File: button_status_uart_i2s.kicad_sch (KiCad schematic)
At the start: 14 parts, among them CN10 JST_ZH_6PIN_1A_250V, CN8 4P JST ZH, CN9 4P JST ZH

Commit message: commit before updating to LiveAstra lib
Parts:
- added R9: 10k, Resistor_SMD:R_0402_1005Metric, symbol EASYEDA2KICAD:R_10kOhm_0402_62mW
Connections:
- net GPIO_12_BUTTON: now also R9.2; no longer CN9.2
- net STATUS_LED_CONN: now reaches CN9.4, R33.2
- new net: CN9.2, R9.1
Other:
- moved on the sheet: R33
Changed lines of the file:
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@@
 	(paper "A4")
+	(junction
+		(at 127 66.04)
+		(diameter 0)
+		(color 0 0 0 0)
+	)
 	(junction
 		(at 88.9 121.92)
@@
 	)
 	(junction
-		(at 88.9 66.04)
+		(at 101.6 66.04)
 		(diameter 0)
 		(color 0 0 0 0)
 	)
 	(junction
-		(at 127 66.04)
+		(at 88.9 66.04)
 		(diameter 0)
 		(color 0 0 0 0)
@@
 	)
 	(junction
-		(at 101.6 66.04)
-		(diameter 0)
-		(color 0 0 0 0)
-	)
-	(junction
 		(at 88.9 154.94)
 		(diameter 0)
@@
 	(wire
 		(pts
-			(xy 127 66.04) (xy 167.64 66.04)
+			(xy 127 66.04) (xy 132.08 66.04)
 		)
 		(stroke
@@
 	(wire
 		(pts
-			(xy 88.9 96.52) (xy 114.3 96.52)
+			(xy 88.9 96.52) (xy 109.22 96.52)
 		)
 		(stroke
@@
 	(wire
 		(pts
+			(xy 142.24 66.04) (xy 167.64 66.04)
+		)
+		(stroke
+			(width 0)
+			(type default)
+		)
+	)
+	(wire
+		(pts
 			(xy 88.9 121.92) (xy 167.64 121.92)
 		)
@@
 	(wire
 		(pts
+			(xy 101.6 66.04) (xy 127 66.04)
+		)
+		(stroke
+			(width 0)
+			(type default)
+		)
+	)
+	(wire
+		(pts
 			(xy 127 81.28) (xy 127 78.74)
 		)
@@
 	(wire
 		(pts
-			(xy 101.6 66.04) (xy 127 66.04)
-		)
-		(stroke
-			(width 0)
-			(type default)
-		)
-	)
-	(wire
-		(pts
 			(xy 88.9 93.98) (xy 88.9 96.52)
 		)
@@
 	(wire
 		(pts
-			(xy 124.46 96.52) (xy 162.56 96.52)
+			(xy 119.38 96.52) (xy 162.56 96.52)
 		)
 		(stroke
@@
 			(width 0)
 			(type default)
+		)
+	)
+	(label "STATUS_LED_CONN"
+		(at 127 96.52 0)
+		(fields_autoplaced yes)
+		(effects
+			(font
+				(size 1.27 1.27)
+			)
+			(justify left bottom)
 		)
 	)
@@
 		(on_board yes)
 		(dnp no)
-		(property "Reference" "#PWR079"
+		(property "Reference" "#PWR79"
 			(at 142.24 113.03 0)
 			(effects
@@
 			(project "AstraControl"
 				(path "/9a751838-dce8-4d69-8a02-736625ac74e7/0db21d8e-3390-4d67-877f-0e5d98e37848/457d2566-de00-4e8c-b469-a22ed41e6193"
-					(reference "#PWR079")
+					(reference "#PWR79")
+					(unit 1)
+				)
+			)
+		)
+	)
+	(symbol
+		(lib_id "EASYEDA2KICAD:R_10kOhm_0402_62mW")
+		(at 137.16 66.04 180)
+		(unit 1)
+		(exclude_from_sim no)
+		(in_bom yes)
+		(on_board yes)
+		(dnp no)
+		(fields_autoplaced yes)
+		(property "Reference" "R9"
+			(at 137.16 57.15 0)
+			(effects
+				(font
+					(size 1.27 1.27)
+				)
+			)
+		)
+		(property "Value" "10k"
+			(at 137.16 59.69 0)
+			(effects
+				(font
+					(size 1.27 1.27)
+					(bold yes)
+				)
+			)
+		)
+		(property "Footprint" "Resistor_SMD:R_0402_1005Metric"
+			(at 137.16 53.34 0)
+			(effects
+				(font
+					(size 1.27 1.27)
+				)
+				(hide yes)
+			)
+		)
+		(property "Datasheet" "https://wmsc.lcsc.com/wmsc/upload/file/pdf/v2/lcsc/2206010100_UNI-ROYAL-Uniroyal-Elec-0402WGF1002TCE_C25744.pdf"
+			(at 137.16 57.15 0)
+			(effects
+				(font
+					(size 1.27 1.27)
+				)
+				(hide yes)
+			)
+		)
+		(property "Description" "Thick Film Resistors"
+			(at 137.16 60.96 0)
+			(effects
+				(font
+					(size 1.27 1.27)
+				)
+				(hide yes)
+			)
+		)
+		(property "LCSC Part" "C25744"
+			(at 137.16 49.53 0)
+			(effects
+				(font
+					(size 1.27 1.27)
+				)
+				(hide yes)
+			)
+		)
+		(property "Extra Values" "50V ±1% 0402 62mW"
+			(at 137.16 62.23 0)
+			(effects
+				(font
+					(size 0.762 0.762)
+					(bold yes)
+				)
+			)
+		)
+		(pin "2"
+		)
+		(pin "1"
+		)
+		(instances
+			(project "AstraControl"
+				(path "/9a751838-dce8-4d69-8a02-736625ac74e7/0db21d8e-3390-4d67-877f-0e5d98e37848/457d2566-de00-4e8c-b469-a22ed41e6193"
+					(reference "R9")
 					(unit 1)
 				)
@@
 	(symbol
 		(lib_id "EASYEDA2KICAD:R_0Ohm_0805_125mW")
-		(at 119.38 96.52 0)
+		(at 114.3 96.52 0)
 		(unit 1)
 		(exclude_from_sim no)
@@
 		(dnp no)
 		(property "Reference" "R33"
-			(at 119.38 88.9 0)
+			(at 114.3 88.9 0)
 			(effects
 				(font
@@
 		)
 		(property "Value" "0"
-			(at 119.38 91.44 0)
+			(at 114.3 91.44 0)
 			(effects
 				(font
@@
 		)
 		(property "Footprint" "Resistor_SMD:R_0805_2012Metric_Pad1.20x1.40mm_HandSolder"
-			(at 119.38 109.22 0)
+			(at 114.3 109.22 0)
 			(effects
 				(font
@@
 		)
 		(property "Datasheet" "https://lcsc.com/product-detail/Chip-Resistor-Surface-Mount-UniOhm_0R-0R0-1_C17477.html"
-			(at 119.38 105.41 0)
+			(at 114.3 105.41 0)
 			(effects
 				(font
@@
 		)
 		(property "Description" "Thick Film Resistors"
-			(at 119.38 101.6 0)
+			(at 114.3 101.6 0)
 			(effects
 				(font
@@
 		)
 		(property "LCSC Part" "C17477"
-			(at 119.38 113.03 0)
+			(at 114.3 113.03 0)
 			(effects
 				(font
@@
 		)
 		(property "Extra Values" "150V ±1% 0805"
-			(at 119.38 93.98 0)
+			(at 114.3 93.98 0)
 			(effects
 				(font
@@
 		(dnp no)
 		(fields_autoplaced yes)
-		(property "Reference" "#PWR083"
+		(property "Reference" "#PWR83"
 			(at 152.4 118.11 0)
 			(effects
@@
 			(project "AstraControl"
 				(path "/9a751838-dce8-4d69-8a02-736625ac74e7/0db21d8e-3390-4d67-877f-0e5d98e37848/457d2566-de00-4e8c-b469-a22ed41e6193"
-					(reference "#PWR083")
+					(reference "#PWR83")
 					(unit 1)
 				)
@@
 		(dnp no)
 		(fields_autoplaced yes)
-		(property "Reference" "#PWR076"
+		(property "Reference" "#PWR76"
 			(at 101.6 87.63 0)
 			(effects
@@
 			(project "AstraControl"
 				(path "/9a751838-dce8-4d69-8a02-736625ac74e7/0db21d8e-3390-4d67-877f-0e5d98e37848/457d2566-de00-4e8c-b469-a22ed41e6193"
-					(reference "#PWR076")
+					(reference "#PWR76")
 					(unit 1)
 				)
@@
 		(dnp no)
 		(fields_autoplaced yes)
-		(property "Reference" "#PWR077"
+		(property "Reference" "#PWR77"
 			(at 127 87.63 0)
 			(effects
@@
 			(project "AstraControl"
 				(path "/9a751838-dce8-4d69-8a02-736625ac74e7/0db21d8e-3390-4d67-877f-0e5d98e37848/457d2566-de00-4e8c-b469-a22ed41e6193"
-					(reference "#PWR077")
+					(reference "#PWR77")
 					(unit 1)
 				)

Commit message: Updated library name, updated and verified all footprints
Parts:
- C22: symbol EASYEDA2KICAD:C_100nF_X7R_0402 -> LiveAstra:C_100nF_X7R_0402
- CN10: symbol EASYEDA2KICAD:JST_ZH_6PIN_1A_250V -> LiveAstra:JST_ZH_6PIN_1A_250V
- CN8, CN9: symbol EASYEDA2KICAD:JST_ZH_4PIN_1A_50V -> LiveAstra:JST_ZH_4PIN_1A_50V
- R32, R9: symbol EASYEDA2KICAD:R_10kOhm_0402_62mW -> LiveAstra:R_10kOhm_0402_62mW
- R33: symbol EASYEDA2KICAD:R_0Ohm_0805_125mW -> LiveAstra:R_0Ohm_0805_125mW
- TP60, TP61, TP62, TP63, TP64, TP65, TP66, TP67: symbol EASYEDA2KICAD:TestPoint_Thimble -> LiveAstra:TestPoint_Thimble
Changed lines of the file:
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@@
 	)
 	(symbol
-		(lib_id "EASYEDA2KICAD:TestPoint_Thimble")
+		(lib_id "LiveAstra:TestPoint_Thimble")
 		(at 88.9 119.38 0)
 		(unit 1)
@@
 	)
 	(symbol
-		(lib_id "EASYEDA2KICAD:JST_ZH_4PIN_1A_50V")
+		(lib_id "LiveAstra:JST_ZH_4PIN_1A_50V")
 		(at 172.72 38.1 0)
 		(unit 1)
@@
 	)
 	(symbol
-		(lib_id "EASYEDA2KICAD:TestPoint_Thimble")
+		(lib_id "LiveAstra:TestPoint_Thimble")
 		(at 88.9 63.5 0)
 		(unit 1)
@@
 	)
 	(symbol
-		(lib_id "EASYEDA2KICAD:TestPoint_Thimble")
+		(lib_id "LiveAstra:TestPoint_Thimble")
 		(at 88.9 93.98 0)
 		(unit 1)
@@
 	)
 	(symbol
-		(lib_id "EASYEDA2KICAD:TestPoint_Thimble")
+		(lib_id "LiveAstra:TestPoint_Thimble")
 		(at 88.9 167.64 0)
 		(unit 1)
@@
 	)
 	(symbol
-		(lib_id "EASYEDA2KICAD:C_100nF_X7R_0402")
+		(lib_id "LiveAstra:C_100nF_X7R_0402")
 		(at 127 73.66 90)
 		(unit 1)
@@
 		(on_board yes)
 		(dnp no)
-		(property "Reference" "#PWR79"
+		(property "Reference" "#PWR079"
 			(at 142.24 113.03 0)
 			(effects
@@
 			(project "AstraControl"
 				(path "/9a751838-dce8-4d69-8a02-736625ac74e7/0db21d8e-3390-4d67-877f-0e5d98e37848/457d2566-de00-4e8c-b469-a22ed41e6193"
-					(reference "#PWR79")
-					(unit 1)
-				)
-			)
-		)
-	)
-	(symbol
-		(lib_id "EASYEDA2KICAD:R_10kOhm_0402_62mW")
+					(reference "#PWR079")
+					(unit 1)
+				)
+			)
+		)
+	)
+	(symbol
+		(lib_id "LiveAstra:R_10kOhm_0402_62mW")
 		(at 137.16 66.04 180)
 		(unit 1)
@@
 	)
 	(symbol
-		(lib_id "EASYEDA2KICAD:JST_ZH_4PIN_1A_50V")
+		(lib_id "LiveAstra:JST_ZH_4PIN_1A_50V")
 		(at 172.72 68.58 0)
 		(unit 1)
@@
 	)
 	(symbol
-		(lib_id "EASYEDA2KICAD:TestPoint_Thimble")
+		(lib_id "LiveAstra:TestPoint_Thimble")
 		(at 88.9 137.16 0)
 		(unit 1)
@@
 	)
 	(symbol
-		(lib_id "EASYEDA2KICAD:R_0Ohm_0805_125mW")
+		(lib_id "LiveAstra:R_0Ohm_0805_125mW")
 		(at 114.3 96.52 0)
 		(unit 1)
@@
 	)
 	(symbol
-		(lib_id "EASYEDA2KICAD:R_10kOhm_0402_62mW")
+		(lib_id "LiveAstra:R_10kOhm_0402_62mW")
 		(at 101.6 73.66 90)
 		(unit 1)
@@
 	)
 	(symbol
-		(lib_id "EASYEDA2KICAD:TestPoint_Thimble")
+		(lib_id "LiveAstra:TestPoint_Thimble")
 		(at 127 38.1 0)
 		(unit 1)
@@
 	)
 	(symbol
-		(lib_id "EASYEDA2KICAD:TestPoint_Thimble")
+		(lib_id "LiveAstra:TestPoint_Thimble")
 		(at 88.9 152.4 0)
 		(unit 1)
@@
 		(dnp no)
 		(fields_autoplaced yes)
-		(property "Reference" "#PWR83"
+		(property "Reference" "#PWR083"
 			(at 152.4 118.11 0)
 			(effects
@@
 			(project "AstraControl"
 				(path "/9a751838-dce8-4d69-8a02-736625ac74e7/0db21d8e-3390-4d67-877f-0e5d98e37848/457d2566-de00-4e8c-b469-a22ed41e6193"
-					(reference "#PWR83")
+					(reference "#PWR083")
 					(unit 1)
 				)
@@
 		(dnp no)
 		(fields_autoplaced yes)
-		(property "Reference" "#PWR76"
+		(property "Reference" "#PWR076"
 			(at 101.6 87.63 0)
 			(effects
@@
 			(project "AstraControl"
 				(path "/9a751838-dce8-4d69-8a02-736625ac74e7/0db21d8e-3390-4d67-877f-0e5d98e37848/457d2566-de00-4e8c-b469-a22ed41e6193"
-					(reference "#PWR76")
+					(reference "#PWR076")
 					(unit 1)
 				)
@@
 		(dnp no)
 		(fields_autoplaced yes)
-		(property "Reference" "#PWR77"
+		(property "Reference" "#PWR077"
 			(at 127 87.63 0)
 			(effects
@@
 			(project "AstraControl"
 				(path "/9a751838-dce8-4d69-8a02-736625ac74e7/0db21d8e-3390-4d67-877f-0e5d98e37848/457d2566-de00-4e8c-b469-a22ed41e6193"
-					(reference "#PWR77")
-					(unit 1)
-				)
-			)
-		)
-	)
-	(symbol
-		(lib_id "EASYEDA2KICAD:JST_ZH_6PIN_1A_250V")
+					(reference "#PWR077")
+					(unit 1)
+				)
+			)
+		)
+	)
+	(symbol
+		(lib_id "LiveAstra:JST_ZH_6PIN_1A_250V")
 		(at 172.72 124.46 0)
 		(unit 1)
@@
 	)
 	(symbol
-		(lib_id "EASYEDA2KICAD:TestPoint_Thimble")
+		(lib_id "LiveAstra:TestPoint_Thimble")
 		(at 88.9 43.18 0)
 		(unit 1)

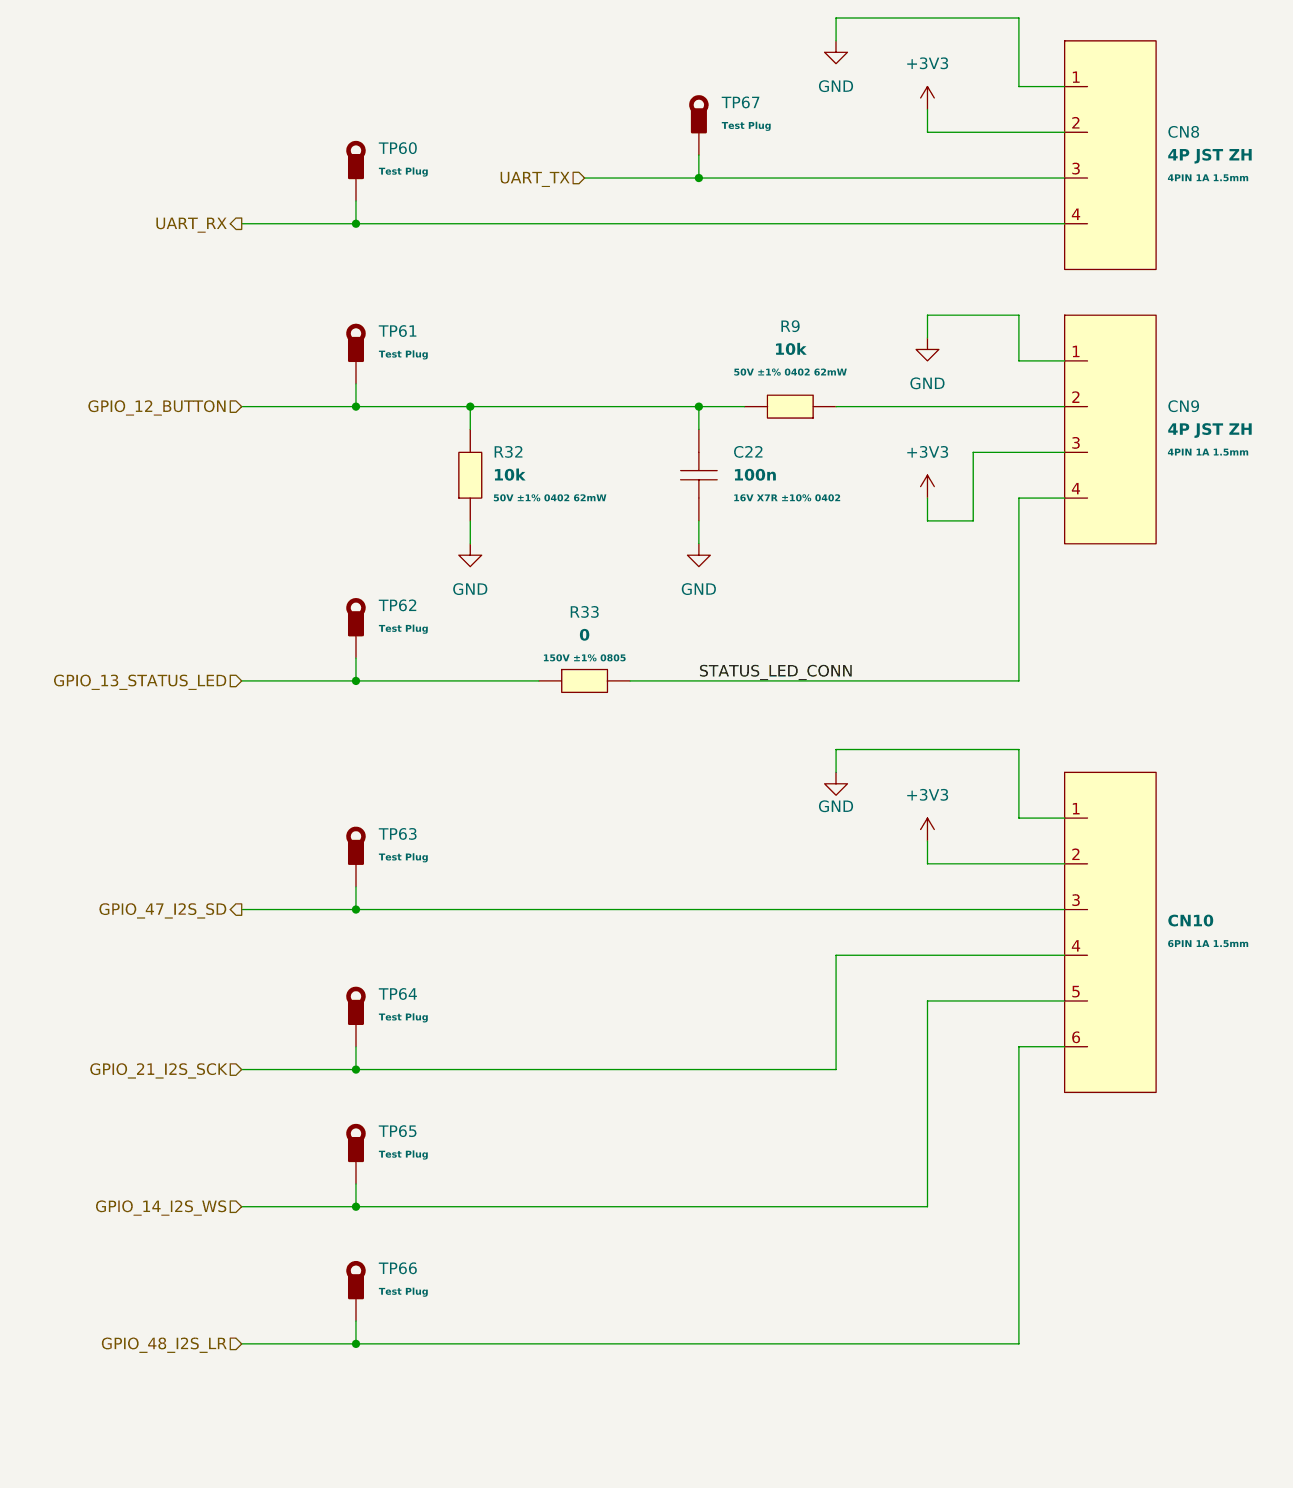
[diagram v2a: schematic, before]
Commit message: Finished layout no drc or erc errors
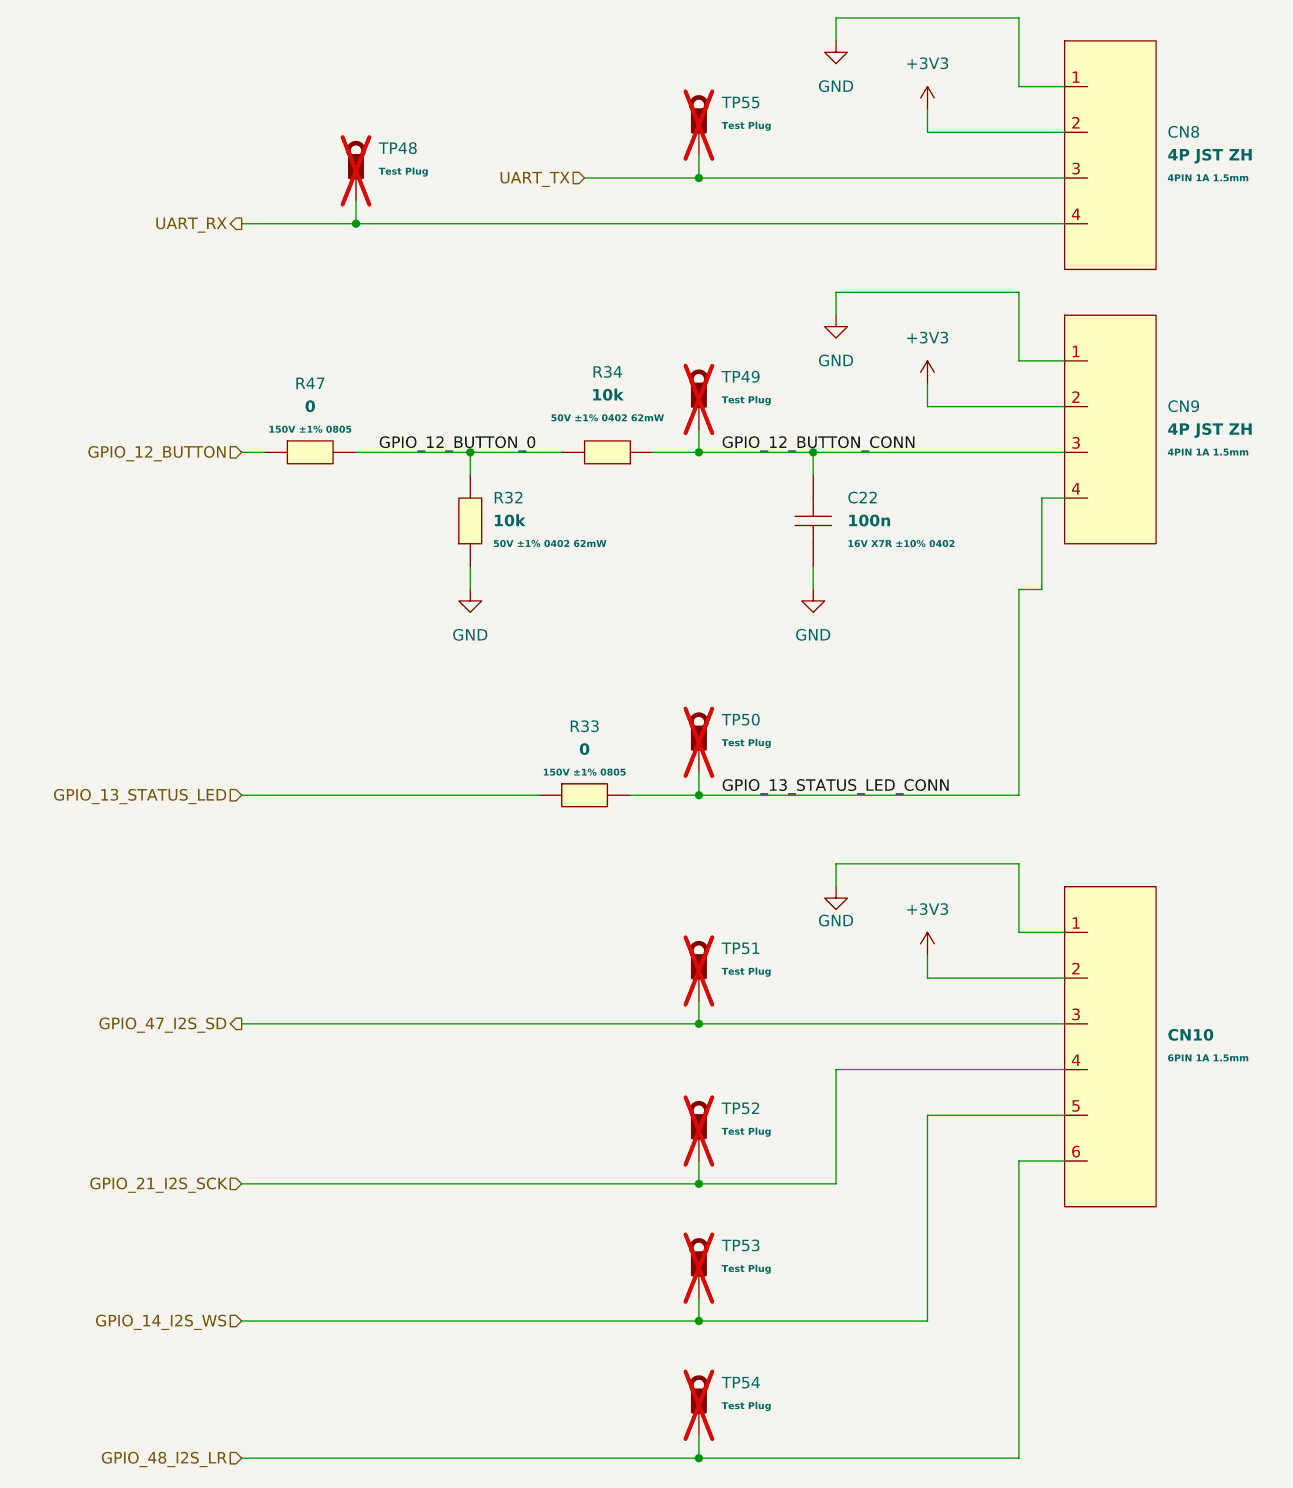
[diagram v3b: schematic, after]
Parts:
- added R47: 0, LiveAstra:R_0805_2012Metric_Pad1.20x1.40mm_HandSolder, symbol LiveAstra:R_0Ohm_0805_125mW
- C22: footprint Capacitor_SMD:C_0402_1005Metric -> LiveAstra:C_0402_1005Metric
- CN10: footprint Connector_JST:JST_ZH_B6B-ZR_1x06_P1.50mm_Vertical -> LiveAstra:JST_ZH_B6B-ZR_1x06_P1.50mm_Vertical; LCSC Part C131342 -> C157984
- CN8, CN9: footprint Connector_JST:JST_ZH_B4B-ZR_1x04_P1.50mm_Vertical -> LiveAstra:JST_ZH_B4B-ZR_1x04_P1.50mm_Vertical
- R32: footprint Resistor_SMD:R_0402_1005Metric -> LiveAstra:R_0402_1005Metric
- R33: footprint Resistor_SMD:R_0805_2012Metric_Pad1.20x1.40mm_HandSolder -> LiveAstra:R_0805_2012Metric_Pad1.20x1.40mm_HandSolder
- R34: renamed from R9; footprint Resistor_SMD:R_0402_1005Metric -> LiveAstra:R_0402_1005Metric
- TP48: renamed from TP60; footprint TestPoint:TestPoint_Loop_D3.50mm_Drill0.9mm_Beaded -> LiveAstra:TestPoint_Loop_D3.50mm_Drill0.9mm_Beaded; now not fitted; now left out of the parts list
- TP49: renamed from TP61; footprint TestPoint:TestPoint_Loop_D3.50mm_Drill0.9mm_Beaded -> LiveAstra:TestPoint_Loop_D3.50mm_Drill0.9mm_Beaded; now not fitted; now left out of the parts list
- TP50: renamed from TP62; footprint TestPoint:TestPoint_Loop_D3.50mm_Drill0.9mm_Beaded -> LiveAstra:TestPoint_Loop_D3.50mm_Drill0.9mm_Beaded; now not fitted; now left out of the parts list
- TP51: renamed from TP63; footprint TestPoint:TestPoint_Loop_D3.50mm_Drill0.9mm_Beaded -> LiveAstra:TestPoint_Loop_D3.50mm_Drill0.9mm_Beaded; now not fitted; now left out of the parts list
- TP52: renamed from TP64; footprint TestPoint:TestPoint_Loop_D3.50mm_Drill0.9mm_Beaded -> LiveAstra:TestPoint_Loop_D3.50mm_Drill0.9mm_Beaded; now not fitted; now left out of the parts list
- TP53: renamed from TP65; footprint TestPoint:TestPoint_Loop_D3.50mm_Drill0.9mm_Beaded -> LiveAstra:TestPoint_Loop_D3.50mm_Drill0.9mm_Beaded; now not fitted; now left out of the parts list
- TP54: renamed from TP66; footprint TestPoint:TestPoint_Loop_D3.50mm_Drill0.9mm_Beaded -> LiveAstra:TestPoint_Loop_D3.50mm_Drill0.9mm_Beaded; now not fitted; now left out of the parts list
- TP55: renamed from TP67; footprint TestPoint:TestPoint_Loop_D3.50mm_Drill0.9mm_Beaded -> LiveAstra:TestPoint_Loop_D3.50mm_Drill0.9mm_Beaded; now not fitted; now left out of the parts list
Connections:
- net +3V3: now also CN9.2; no longer CN9.3
- net GPIO_12_BUTTON: now also R47.1; no longer C22.2, R32.2, R34.2, TP49.1
- net GPIO_13_STATUS_LED: no longer TP50.1
- net GPIO_12_BUTTON_CONN: now reaches R34.1
- net GPIO_12_BUTTON_CONN: now also C22.2, CN9.3, TP49.1; no longer CN9.2
- net STATUS_LED_CONN renamed GPIO_13_STATUS_LED_CONN
- net GPIO_13_STATUS_LED_CONN: now also TP50.1
- new net GPIO_12_BUTTON_0: R32.2, R34.2, R47.2
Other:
- moved on the sheet: C22, CN10, R32, R33, R34
